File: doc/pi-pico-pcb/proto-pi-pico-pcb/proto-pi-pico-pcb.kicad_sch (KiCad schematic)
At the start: 14 parts

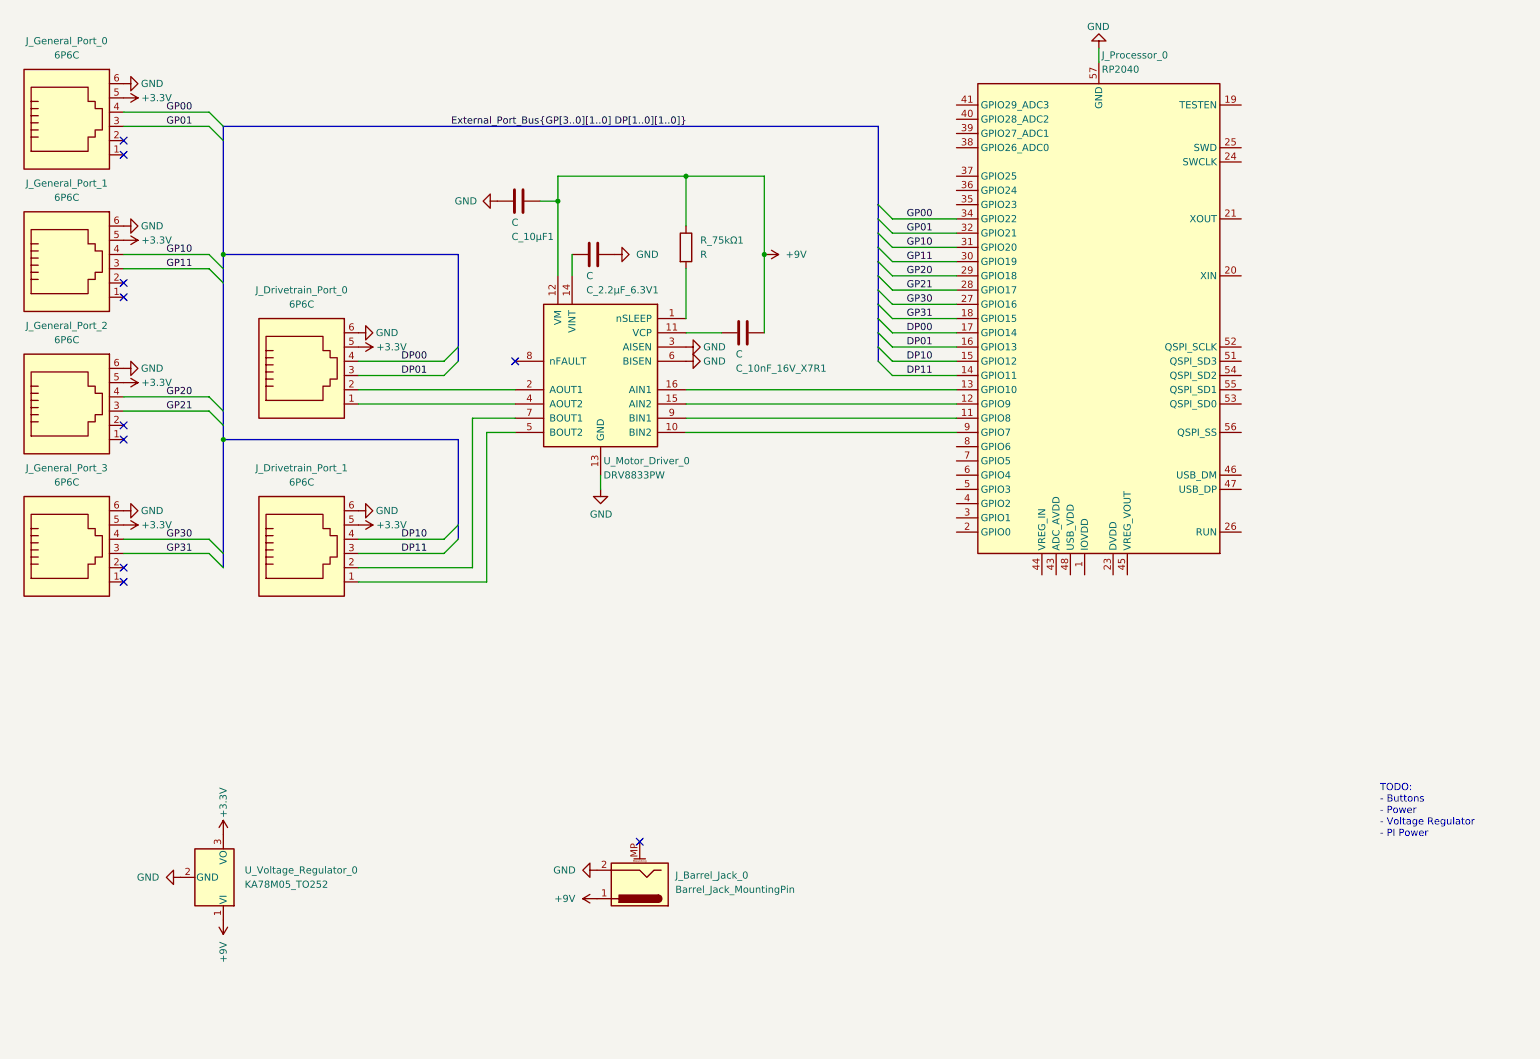
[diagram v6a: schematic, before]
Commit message: added 2 new drivetrain ports, 2nd driver, and push buttons
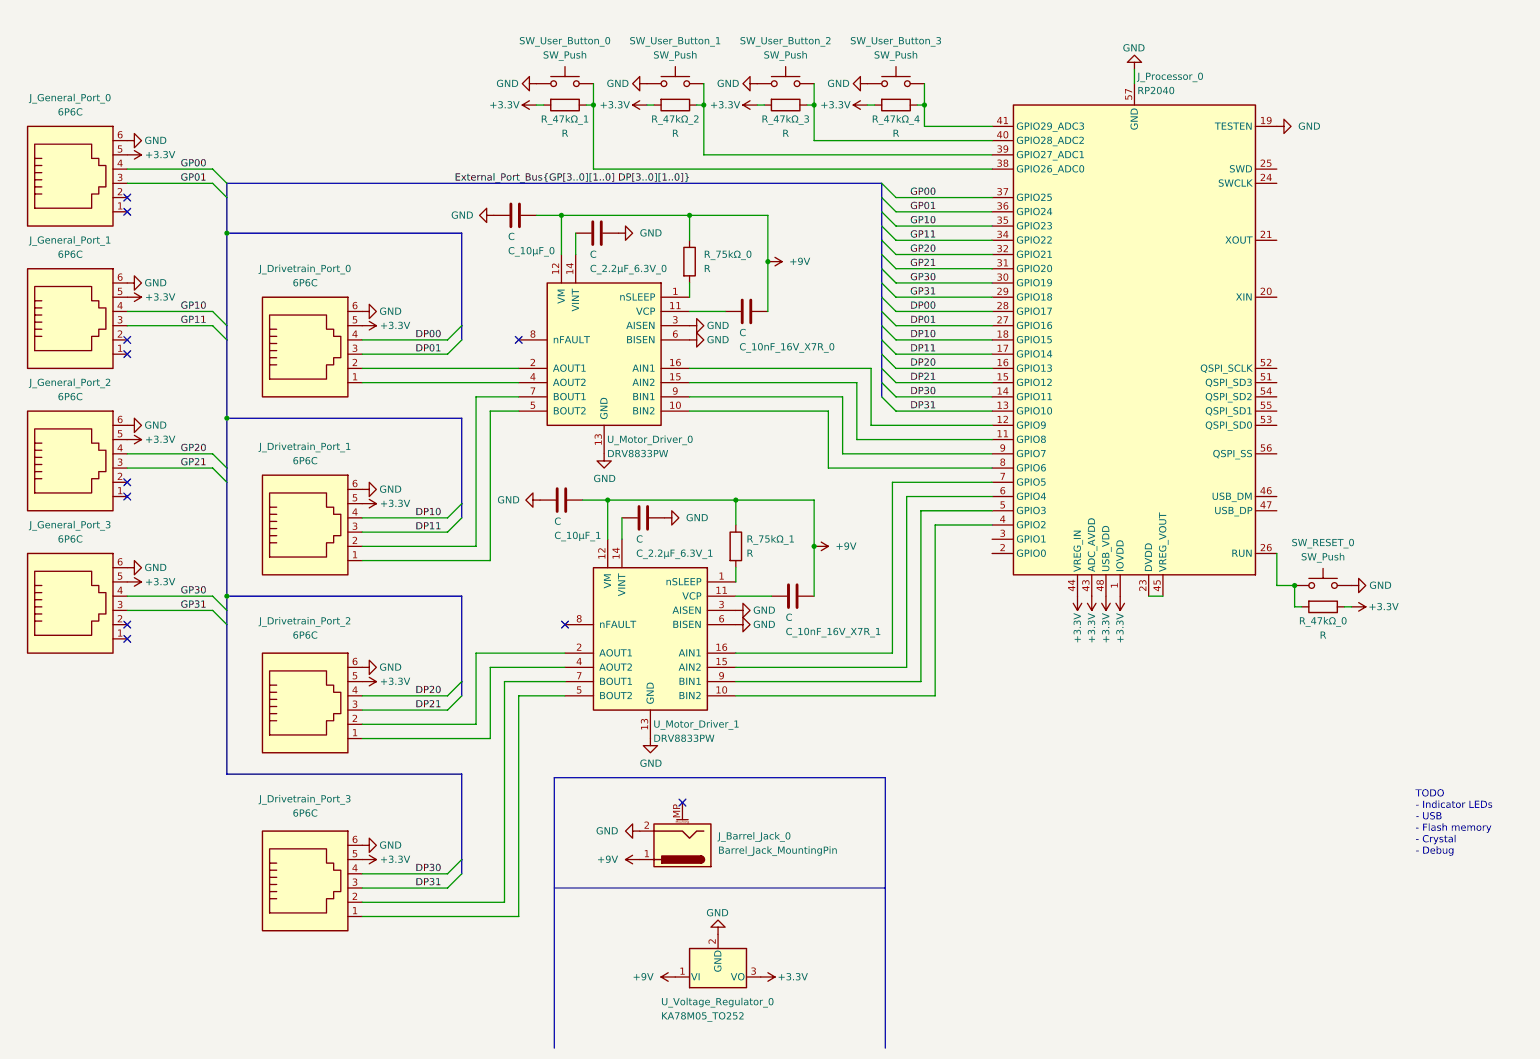
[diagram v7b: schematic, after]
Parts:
- added C_10nF_16V_X7R_1, C_10μF_1, C_2.2μF_6.3V_1: C, Capacitor_SMD:CP_Elec_3x5.3, symbol Device:C
- added J_Drivetrain_Port_2, J_Drivetrain_Port_3: 6P6C, Connector_RJ:RJ12_Amphenol_54601, symbol Connector:6P6C
- added R_47kΩ_0, R_47kΩ_1, R_47kΩ_2, R_47kΩ_3, R_47kΩ_4, R_75kΩ_1: R, Resistor_SMD:R_0201_0603Metric, symbol Device:R
- added SW_RESET_0, SW_User_Button_0, SW_User_Button_1, SW_User_Button_2, SW_User_Button_3: SW_Push, symbol Switch:SW_Push
- added U_Motor_Driver_1: DRV8833PW, Package_SO:TSSOP-16_4.4x5mm_P0.65mm, symbol Driver_Motor:DRV8833PW
- renumbered C_10nF_16V_X7R1 to C_10nF_16V_X7R_0, C_10μF1 to C_10μF_0, C_2.2μF_6.3V1 to C_2.2μF_6.3V_0, R_75kΩ1 to R_75kΩ_0
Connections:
- net +3.3V: now also J_Processor_0.1 (IOVDD), J_Processor_0.10 (IOVDD), J_Processor_0.22 (IOVDD), J_Processor_0.33 (IOVDD), J_Processor_0.42 (IOVDD), J_Processor_0.43 (ADC_AVDD), J_Processor_0.44 (VREG_IN), J_Processor_0.48 (USB_VDD), J_Processor_0.49 (IOVDD), J_Drivetrain_Port_2.5, J_Drivetrain_Port_3.5, R_47kΩ_0.1, R_47kΩ_1.2, R_47kΩ_2.2, R_47kΩ_3.2, R_47kΩ_4.2
- net +9V: now also C_10nF_16V_X7R_1.1, C_10μF_1.1, R_75kΩ_1.1, U_Motor_Driver_1.12 (VM)
- net DP00: now also J_Processor_0.28 (GPIO17); no longer J_Processor_0.17 (GPIO14)
- net DP01: now also J_Processor_0.27 (GPIO16); no longer J_Processor_0.16 (GPIO13)
- net DP10: now also J_Processor_0.18 (GPIO15); no longer J_Processor_0.15 (GPIO12)
- net DP11: now also J_Processor_0.17 (GPIO14); no longer J_Processor_0.14 (GPIO11)
- net GND: now also J_Processor_0.19 (TESTEN), C_10μF_1.2, C_2.2μF_6.3V_1.1, J_Drivetrain_Port_2.6, J_Drivetrain_Port_3.6, SW_RESET_0.2, SW_User_Button_0.1, SW_User_Button_1.1, SW_User_Button_2.1, SW_User_Button_3.1, U_Motor_Driver_1.13 (GND), U_Motor_Driver_1.3 (AISEN), U_Motor_Driver_1.6 (BISEN)
- net GP00: now also J_Processor_0.37 (GPIO25); no longer J_Processor_0.34 (GPIO22)
- net GP01: now also J_Processor_0.36 (GPIO24); no longer J_Processor_0.32 (GPIO21)
- net GP10: now also J_Processor_0.35 (GPIO23); no longer J_Processor_0.31 (GPIO20)
- net GP11: now also J_Processor_0.34 (GPIO22); no longer J_Processor_0.30 (GPIO19)
- net GP20: now also J_Processor_0.32 (GPIO21); no longer J_Processor_0.29 (GPIO18)
- net GP21: now also J_Processor_0.31 (GPIO20); no longer J_Processor_0.28 (GPIO17)
- net GP30: now also J_Processor_0.30 (GPIO19); no longer J_Processor_0.27 (GPIO16)
- net GP31: now also J_Processor_0.29 (GPIO18); no longer J_Processor_0.18 (GPIO15)
- net at J_Processor_0.11 (GPIO8): now also U_Motor_Driver_0.15 (AIN2); no longer U_Motor_Driver_0.9 (BIN1)
- net at J_Processor_0.12 (GPIO9): now also U_Motor_Driver_0.16 (AIN1); no longer U_Motor_Driver_0.15 (AIN2)
- net DP31: now reaches J_Processor_0.13 (GPIO10)
- net DP31: now also J_Drivetrain_Port_3.3; no longer U_Motor_Driver_0.16 (AIN1)
- net at J_Processor_0.23 (DVDD), J_Processor_0.50 (DVDD): now also J_Processor_0.45 (VREG_VOUT)
- net at J_Processor_0.26 (RUN): now also R_47kΩ_0.2, SW_RESET_0.1
- net at J_Processor_0.38 (GPIO26_ADC0): now also R_47kΩ_1.1, SW_User_Button_0.2
- net at J_Processor_0.39 (GPIO27_ADC1): now also R_47kΩ_2.1, SW_User_Button_1.2
- net at J_Processor_0.4 (GPIO2): now also U_Motor_Driver_1.10 (BIN2)
- net at J_Processor_0.40 (GPIO28_ADC2): now also R_47kΩ_3.1, SW_User_Button_2.2
- net at J_Processor_0.41 (GPIO29_ADC3): now also R_47kΩ_4.1, SW_User_Button_3.2
- net at J_Processor_0.5 (GPIO3): now also U_Motor_Driver_1.9 (BIN1)
- net at J_Processor_0.6 (GPIO4): now also U_Motor_Driver_1.15 (AIN2)
- net at J_Processor_0.7 (GPIO5): now also U_Motor_Driver_1.16 (AIN1)
- net at J_Processor_0.8 (GPIO6): now also U_Motor_Driver_0.10 (BIN2)
- net at J_Processor_0.9 (GPIO7): now also U_Motor_Driver_0.9 (BIN1); no longer U_Motor_Driver_0.10 (BIN2)
- new net: R_75kΩ_1.2, U_Motor_Driver_1.1 (nSLEEP)
- new net: C_10nF_16V_X7R_1.2, U_Motor_Driver_1.11 (VCP)
- new net: C_2.2μF_6.3V_1.2, U_Motor_Driver_1.14 (VINT)
- new net: J_Drivetrain_Port_2.2, U_Motor_Driver_1.2 (AOUT1)
- new net: J_Drivetrain_Port_2.1, U_Motor_Driver_1.4 (AOUT2)
- new net: J_Drivetrain_Port_3.1, U_Motor_Driver_1.5 (BOUT2)
- new net: J_Drivetrain_Port_3.2, U_Motor_Driver_1.7 (BOUT1)
- new net DP20: J_Drivetrain_Port_2.4, J_Processor_0.16 (GPIO13)
- new net DP21: J_Drivetrain_Port_2.3, J_Processor_0.15 (GPIO12)
- new net DP30: J_Drivetrain_Port_3.4, J_Processor_0.14 (GPIO11)
- no-connect marks 10 -> 11
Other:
- note added: "TODO - Indicator LEDs - USB - Flash memory - Crystal - Debug"
- note removed: "TODO: - Buttons - Power - Voltage Regulator - PI Power"
- company: (none) -> PROTO
- title: (none) -> Red Board
- moved on the sheet: C_10nF_16V_X7R_0, C_10μF_0, C_2.2μF_6.3V_0, J_Barrel_Jack_0, J_Drivetrain_Port_0, J_Drivetrain_Port_1, J_General_Port_0, J_General_Port_1, J_General_Port_2, J_General_Port_3, J_Processor_0, R_75kΩ_0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

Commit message: introduced nested sheets
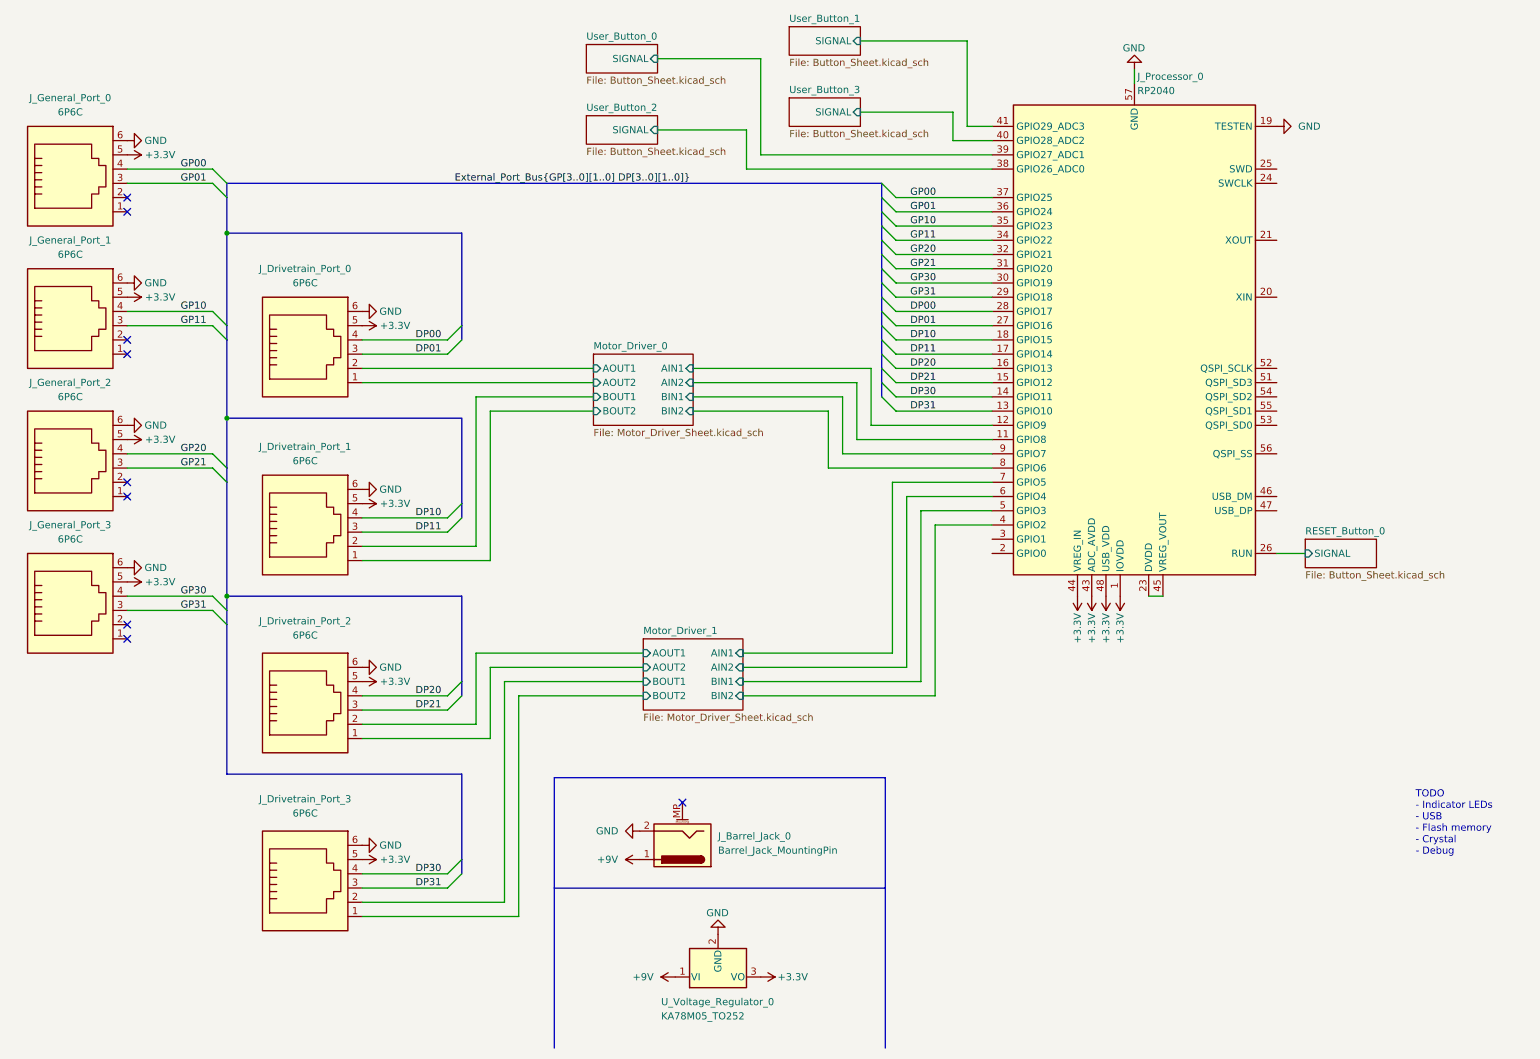
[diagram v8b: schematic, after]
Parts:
- removed C_10nF_16V_X7R_0, C_10nF_16V_X7R_1, C_10μF_0, C_10μF_1, C_2.2μF_6.3V_0, C_2.2μF_6.3V_1: C, Capacitor_SMD:CP_Elec_3x5.3, symbol Device:C
- removed R_47kΩ_0, R_47kΩ_1, R_47kΩ_2, R_47kΩ_3, R_47kΩ_4, R_75kΩ_0, R_75kΩ_1: R, Resistor_SMD:R_0201_0603Metric, symbol Device:R
- removed SW_RESET_0, SW_User_Button_0, SW_User_Button_1, SW_User_Button_2, SW_User_Button_3: SW_Push, symbol Switch:SW_Push
- removed U_Motor_Driver_0, U_Motor_Driver_1: DRV8833PW, Package_SO:TSSOP-16_4.4x5mm_P0.65mm, symbol Driver_Motor:DRV8833PW
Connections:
- net User_Button_1/SIGNAL: now reaches J_Processor_0.41 (GPIO29_ADC3)
- net Motor_Driver_0/AOUT2: now reaches J_Drivetrain_Port_0.1
- net Motor_Driver_0/AOUT1: now reaches J_Drivetrain_Port_0.2
- net Motor_Driver_1/BIN2: now reaches J_Processor_0.4 (GPIO2)
- net Motor_Driver_1/AIN2: now reaches J_Processor_0.6 (GPIO4)
- net Motor_Driver_1/AIN1: now reaches J_Processor_0.7 (GPIO5)
- net Motor_Driver_1/AOUT1: now reaches J_Drivetrain_Port_2.2
- net Motor_Driver_1/AOUT2: now reaches J_Drivetrain_Port_2.1
- net Motor_Driver_1/BOUT2: now reaches J_Drivetrain_Port_3.1
- net Motor_Driver_1/BOUT1: now reaches J_Drivetrain_Port_3.2
- net Motor_Driver_1/BIN1: now reaches J_Processor_0.5 (GPIO3)
- net User_Button_2/SIGNAL: now reaches J_Processor_0.38 (GPIO26_ADC0)
- net Motor_Driver_0/AIN2: now reaches J_Processor_0.11 (GPIO8)
- net Motor_Driver_0/AIN1: now reaches J_Processor_0.12 (GPIO9)
- net RESET_Button_0/SIGNAL: now reaches J_Processor_0.26 (RUN)
- net User_Button_0/SIGNAL: now reaches J_Processor_0.39 (GPIO27_ADC1)
- net User_Button_3/SIGNAL: now reaches J_Processor_0.40 (GPIO28_ADC2)
- net Motor_Driver_0/BIN2: now reaches J_Processor_0.8 (GPIO6)
- net Motor_Driver_0/BIN1: now reaches J_Processor_0.9 (GPIO7)
- net Motor_Driver_0/BOUT2: now reaches J_Drivetrain_Port_1.1
- net Motor_Driver_0/BOUT1: now reaches J_Drivetrain_Port_1.2
- no-connect marks 11 -> 9
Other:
- added sheet Motor_Driver_0 (Motor_Driver_Sheet.kicad_sch)
- added sheet Motor_Driver_1 (Motor_Driver_Sheet.kicad_sch)
- added sheet RESET_Button_0 (Button_Sheet.kicad_sch)
- added sheet User_Button_0 (Button_Sheet.kicad_sch)
- added sheet User_Button_1 (Button_Sheet.kicad_sch)
- added sheet User_Button_2 (Button_Sheet.kicad_sch)
- added sheet User_Button_3 (Button_Sheet.kicad_sch)
